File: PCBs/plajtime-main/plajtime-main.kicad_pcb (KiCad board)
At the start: 6 copper layers, 15.2 x 34 mm, 83 parts, among them J1 RP SWD, J2 RP USB, J3 Internal connector, J4 Display connector, J5 Extention connector, J6 Conn_Coaxial, J7 Battery Connector, J8 Nordic SWD, J9 Conn_Coaxial, U1 W25Q64JWU, U2 W25Q64JWBYIM, U3 TPS628438YKA, U4 MP2664, U5 RP2350A, U6 BMA456, U7 MAX17055, U8 RV-3028-C7, U9 nRF52833_QDxx, Y1 13MHz, Y2 32MHz

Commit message: PCB_main: Add 32.768kHz crystal, Split AUX and USB, retrace changes
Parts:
- removed C28: 0.1uF, Capacitor_SMD:C_0201_0603Metric
- removed J3: Internal connector, Library:CONN12_505066-1222_179x87_MOL
- removed R6, R7: 10k, Resistor_SMD:R_0201_0603Metric
- removed U8: RV-3028-C7, Package_SON:MicroCrystal_C7_SON-8_1.5x3.2mm_P0.9mm
- added C46: TBD, Capacitor_SMD:C_0201_0603Metric, B.Cu at (-11.0, 6.70)
- added C47: TBD, Capacitor_SMD:C_0201_0603Metric, B.Cu at (-8.70, 3.98)
- added J10: Internal connector, Library:5050660822, F.Cu at (-11.4, 1.15)
- added J11: USB, Library:CONN_505066-0622_MOL, F.Cu at (-16.5, 6.65)
- added R13: 300k, Resistor_SMD:R_0201_0603Metric, B.Cu at (-13.9, 0.90)
- added Y3: 32.768kHz Crystal, Crystal:Crystal_SMD_MicroCrystal_CM9V-T1A-2Pin_1.6x1.0mm, B.Cu at (-10.4, 4.70)
- R1: value 10k -> 7.32k
- U1: value W25Q64JWU -> W25Q64JWUUIQ
- moved J8 2.66 mm to (-18.0, 6.93), turned to -160 degrees
- moved C36 0.39 mm to (-13.7, 8.68), turned to 0 degrees
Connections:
- net Net-(U4-VDD) renamed /CHG_VDD
- U9 pad 17: /RTC_INT -> /CHARGER_INT
- U9 pad 2: SCL -> Net-(U9-XL1/P0.00)
- U9 pad 3: SDA -> Net-(U9-XL2/P0.01)
- U9 pad 4: GPU_INT -> SCL
- U9 pad 5: FREEPIN -> SDA
- U9 pad 7: /CHARGER_INT -> GPU_INT
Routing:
- net /CLK_OUT: track 26.8 -> 0.00 mm, vias 2 -> 0
- net USB_D-: track 12.2 -> 2.13 mm, vias 2 -> 0
- net USB_D+: track 10.7 -> 2.13 mm, vias 2 -> 0
- net +5V: track 5.94 -> 11.9 mm
- net /RTC_INT: track 4.40 -> 0.00 mm
- net /CHARGER_INT: track 6.06 -> 9.86 mm, vias 0 -> 2
- net Net-(U9-XL1/P0.00): track 0.00 -> 3.54 mm, vias 0 -> 1
- net SCL: track 29.3 -> 25.9 mm, vias 6 -> 5
- net VSYS: track 14.8 -> 11.5 mm, vias 3 -> 4
- net Net-(U9-XL2/P0.01): track 0.00 -> 2.49 mm, vias 0 -> 1
- net Net-(J8-Pin_1): track 3.37 -> 5.23 mm
- net GPU_INT: track 12.1 -> 13.6 mm
- net +3V: track 28.1 -> 26.7 mm, vias 26 -> 25
- net /SLIDER_INT: track 7.46 -> 8.85 mm
- net Net-(J8-Pin_2): track 3.38 -> 4.68 mm
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
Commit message: Some fixes after v0.4
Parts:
- moved C27 0.72 mm to (-15.8, 3.71), turned to -90 degrees
- moved J10 0.22 mm to (-11.3, 0.94)
- moved L2 0.18 mm to (-18.2, 3.04)
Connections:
- U5 pad 37: /CLK_OUT -> unconnected-(U5-GPIO25-Pad37)
- U9 pad 6: /GAUGE_INT -> GPU_INT
- U9 pad 7: GPU_INT -> /GAUGE_INT
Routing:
- net SCL: track 25.9 -> 32.3 mm
- net /CHARGER_INT: track 9.86 -> 12.2 mm, vias 2 -> 3
- net SDA: track 33.2 -> 31.4 mm, vias 4 -> 5
- net +5V: track 11.9 -> 10.5 mm
- net GPU_INT: track 13.6 -> 12.4 mm, vias 2 -> 0
- net RP_SCL: track 13.8 -> 14.7 mm
- net /SLIDER_INT: track 8.85 -> 8.16 mm
- net RP_SDA: track 13.1 -> 13.7 mm
- net /GAUGE_INT: track 13.6 -> 13.5 mm, vias 2 -> 0
- net GND: track 28.3 -> 28.2 mm, vias 81 -> 84

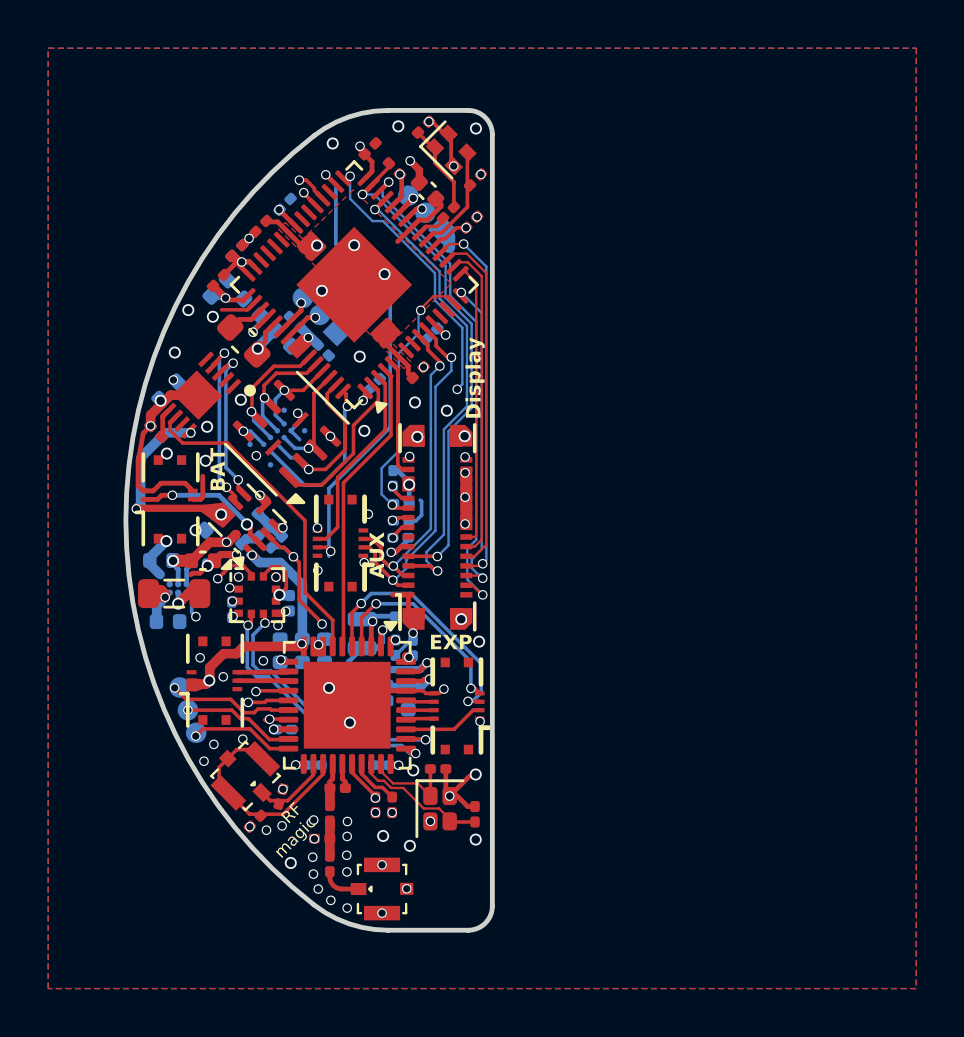
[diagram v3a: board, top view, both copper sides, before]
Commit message: main-pcb: Fix Nordic USB (DECUSB), Improve I2C and RTC crystal routing
Also added labels for some nets, done basic board cleanup
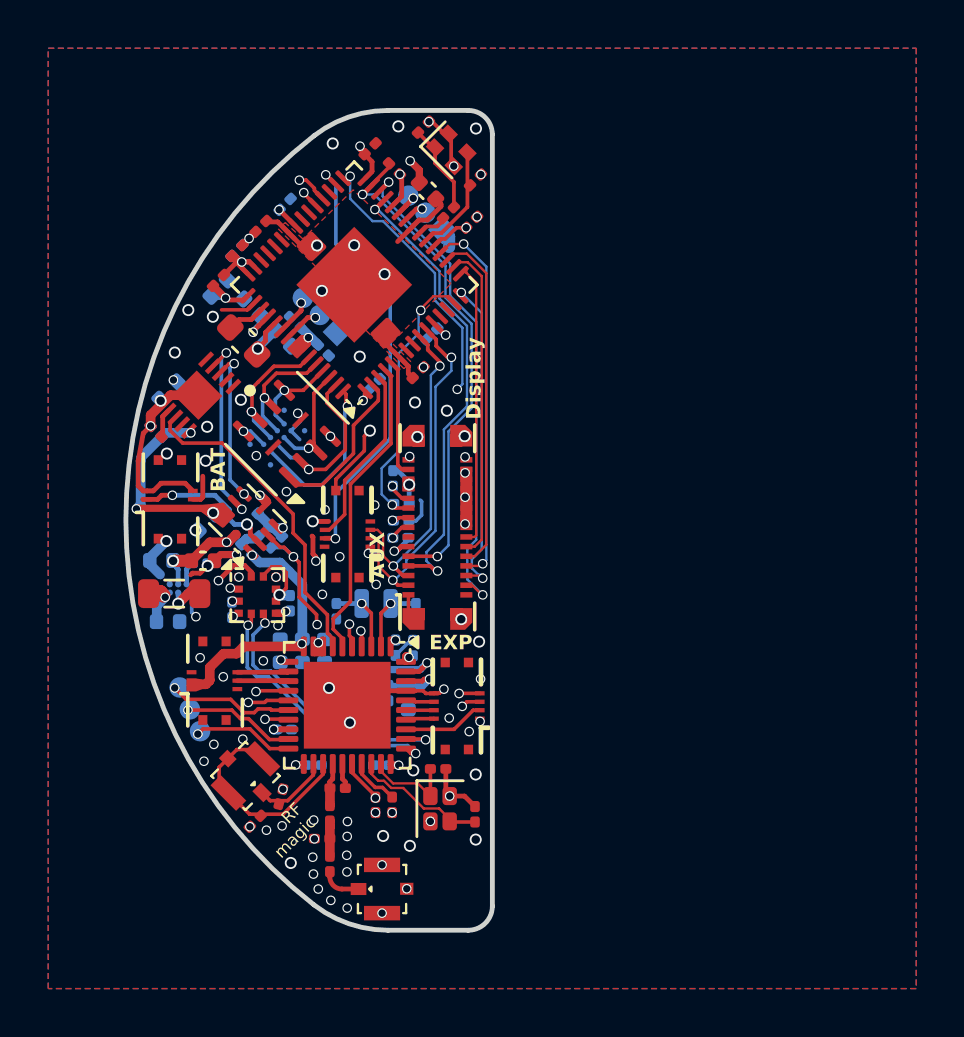
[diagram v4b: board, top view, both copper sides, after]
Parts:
- moved C46 4.06 mm to (-8.17, 3.77)
- moved C47 2.78 mm to (-11.5, 3.77), turned to -90 degrees
- moved C31 1.84 mm to (-12.0, 5.42), turned to -90 degrees
- moved C35 1.84 mm to (-13.8, 5.41), turned to 90 degrees
- moved Y3 1.38 mm to (-9.82, 3.45), turned to 0 degrees
- moved J10 0.47 mm to (-11.0, 0.57)
- moved C17 0.28 mm to (-16.9, 0.08)
- turned J8 to -155 degrees
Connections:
- net Net-(J1-Pin_2) renamed /RP_SWDCLK
- net Net-(J1-Pin_3) renamed /RP_SWDIO
- net Net-(J2-Pin_2) renamed /RP_USB_D+
- net Net-(J2-Pin_3) renamed /RP_USB_D-
- net Net-(J8-Pin_1) renamed /NRF_SWDRST
- net Net-(J8-Pin_2) renamed /NRF_SWDCLK
- net Net-(J8-Pin_3) renamed /NRF_SWDIO
- net Net-(U9-XL1/P0.00) renamed /NRF_XL1
- net Net-(U9-XL2/P0.01) renamed /NRF_XL2
- C35 pad 1: +3V -> /NRF_DECUSB
- U9 pad 11: +3V -> /NRF_DECUSB
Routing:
- net SCL: track 32.3 -> 29.1 mm
- net GND: track 28.2 -> 30.4 mm, vias 84 -> 92
- net SDA: track 31.4 -> 29.2 mm
- net /VIC_INT: track 19.2 -> 18.2 mm
- net /SLIDER_INT: track 8.16 -> 7.57 mm
- net VSYS: track 12.0 -> 12.6 mm
- net /NRF_XL1: track 3.54 -> 3.00 mm
- net +3V: track 26.9 -> 26.4 mm, vias 25 -> 24
- net /NRF_XL2: track 2.49 -> 3.00 mm
- net /NRF_DECUSB: track 0.00 -> 0.35 mm, vias 0 -> 1
- net +5V: vias 3 -> 2

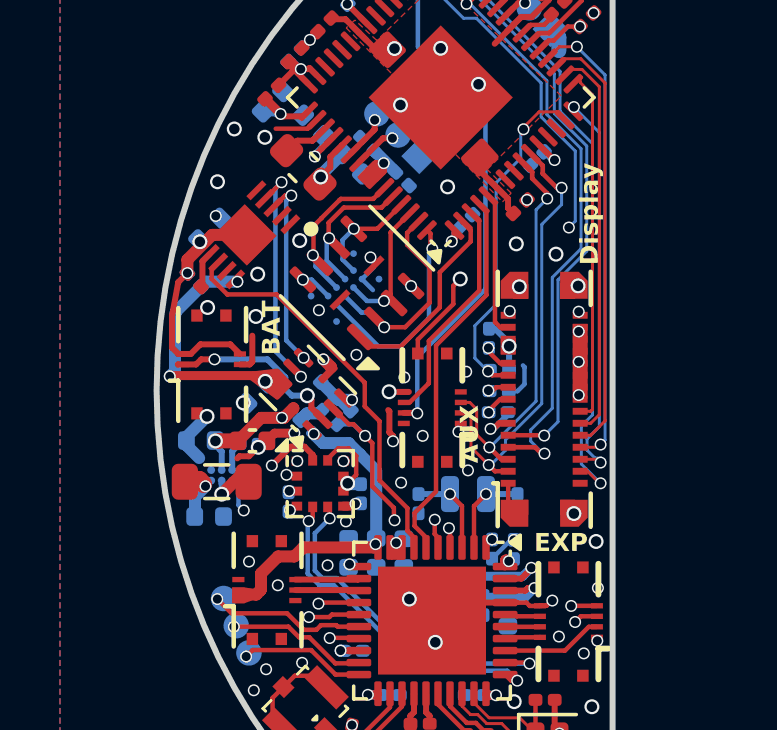
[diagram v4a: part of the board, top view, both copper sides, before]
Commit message: main-pcb: Fix charger shutdown properly
The previous fix used VDD (internal charger voltage), which was
not allowed. This fix uses the battery directly instead, to create
a pull-up on the INT pin. Additionally, a resistor is needed between
the sensing pin and the charger INT pin, because the nRF was pulling
it too hard, exceeding the minimum pin threshold. Therefore,
the resistor values should be calculated with this in mind.
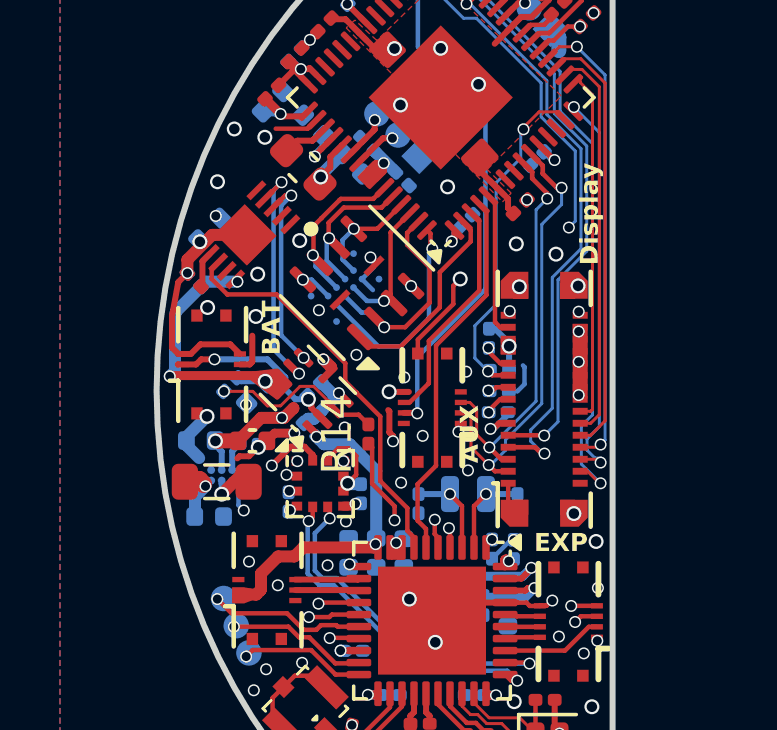
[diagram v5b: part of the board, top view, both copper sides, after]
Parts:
- added R14: TBD, Resistor_SMD:R_0201_0603Metric, F.Cu at (-13.1, 1.45)
- R13: value 300k -> TBD
- moved R13 3.94 mm to (-17.7, -0.20)
- moved C2 0.15 mm to (-15.1, 1.32)
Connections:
- R13 pad 1: /CHG_VDD -> +BATT
- R13 pad 2: /CHARGER_INT -> Net-(U4-INT)
- U4 pad 3: /CHARGER_INT -> Net-(U4-INT)
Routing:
- net Net-(U4-INT): track 0.00 -> 5.86 mm, vias 0 -> 1
- net /CHARGER_INT: track 12.3 -> 9.53 mm, vias 3 -> 2
- net /CHG_VDD: track 2.73 -> 1.11 mm
- net +BATT: track 7.84 -> 8.82 mm
- net GND: track 30.4 -> 30.3 mm, vias 92 -> 93
